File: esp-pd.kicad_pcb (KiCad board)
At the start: 4 copper layers, 83 parts, among them J1 USB C Power, J2 USB C Data, J3 Power Out, J4 ESP PD Board pins, Q1 IRF7416, Q2 MMBT3904, SW1 Boot, SW2 Reset, SW3 Up, SW4 Down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

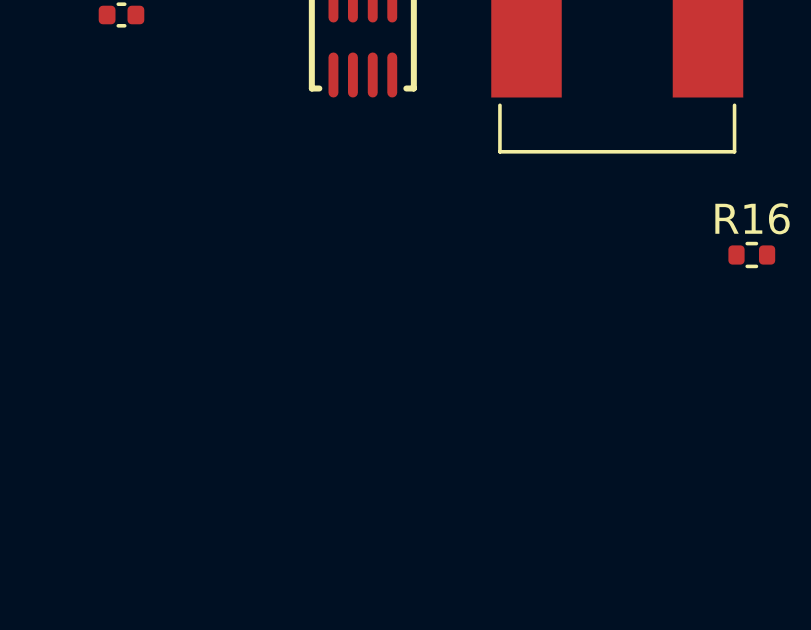
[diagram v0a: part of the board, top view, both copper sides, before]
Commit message: added BST diode
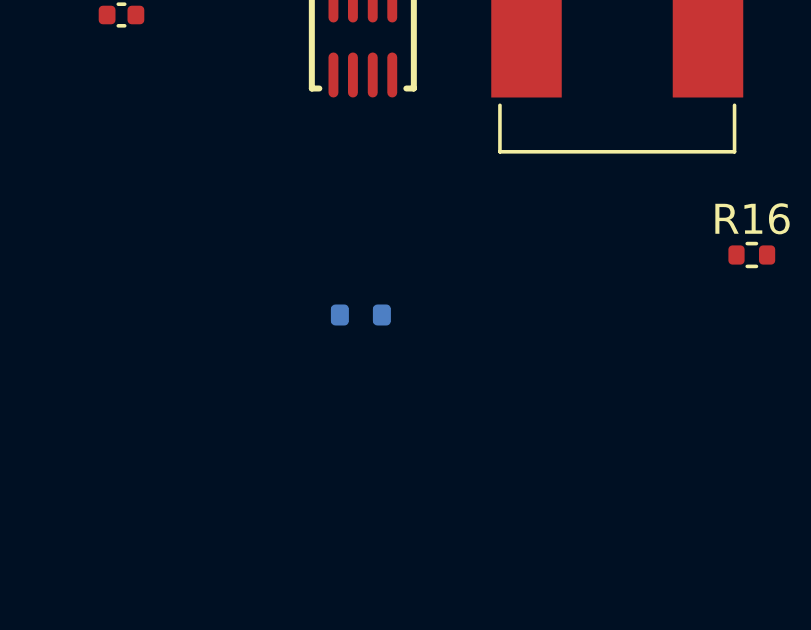
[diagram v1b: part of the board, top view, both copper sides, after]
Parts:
- added D5: 1N4148, Diode_SMD:D_SOD-523, B.Cu at (45.5, 137.0)

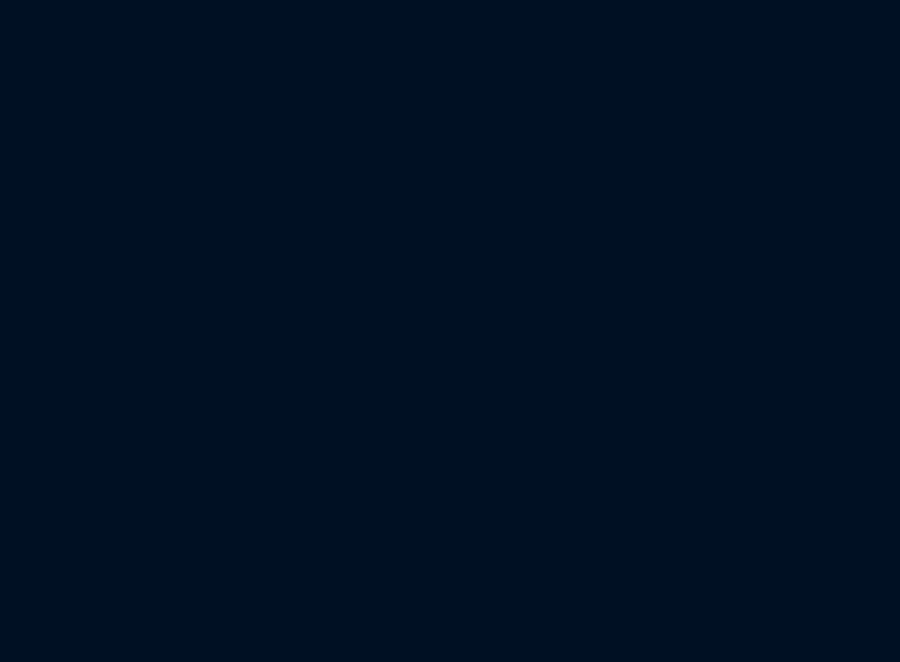
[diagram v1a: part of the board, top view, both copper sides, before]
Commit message: added INA226
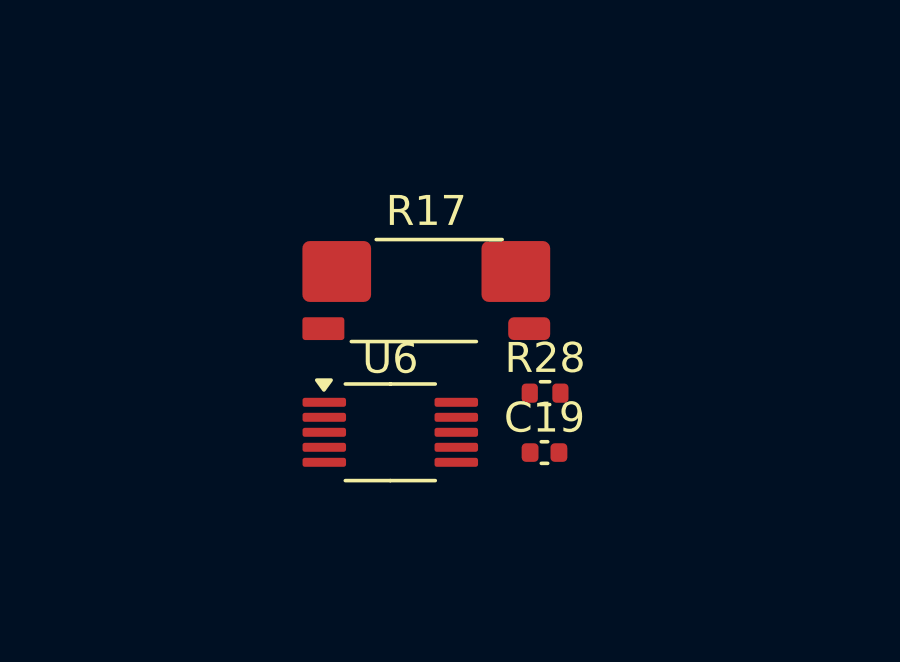
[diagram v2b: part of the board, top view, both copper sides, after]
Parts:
- added C19: 0.1 uF, Capacitor_SMD:C_0402_1005Metric, F.Cu at (93.0, 169.0)
- added R17: 0.010R, pb_board:R_Shunt_Vishay_WSK2512_6332Metric_new, F.Cu at (89.1, 163.6)
- added R28: 0, Resistor_SMD:R_0402_1005Metric, F.Cu at (93.0, 167.0)
- added U6: INA226, Package_SO:VSSOP-10_3x3mm_P0.5mm, F.Cu at (87.9, 168.3)
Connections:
- D2 pad 3: VBUS -> VOUT
- J3 pad 1: VBUS -> VOUT
- J3 pad 2: VOUT -> VMOS
- Q1 pad 1: VBUS -> VOUT
- Q1 pad 2: VBUS -> VOUT
- Q1 pad 3: VBUS -> VOUT
- Q1 pad 5: VOUT -> VMOS
- Q1 pad 6: VOUT -> VMOS
- Q1 pad 7: VOUT -> VMOS
- Q1 pad 8: VOUT -> VMOS
- R20 pad 1: VBUS -> VOUT
